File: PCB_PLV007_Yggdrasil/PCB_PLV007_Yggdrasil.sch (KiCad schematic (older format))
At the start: 26 parts, among them J1 Conn_01x12, U7 BME280, U8 SN65HVD232

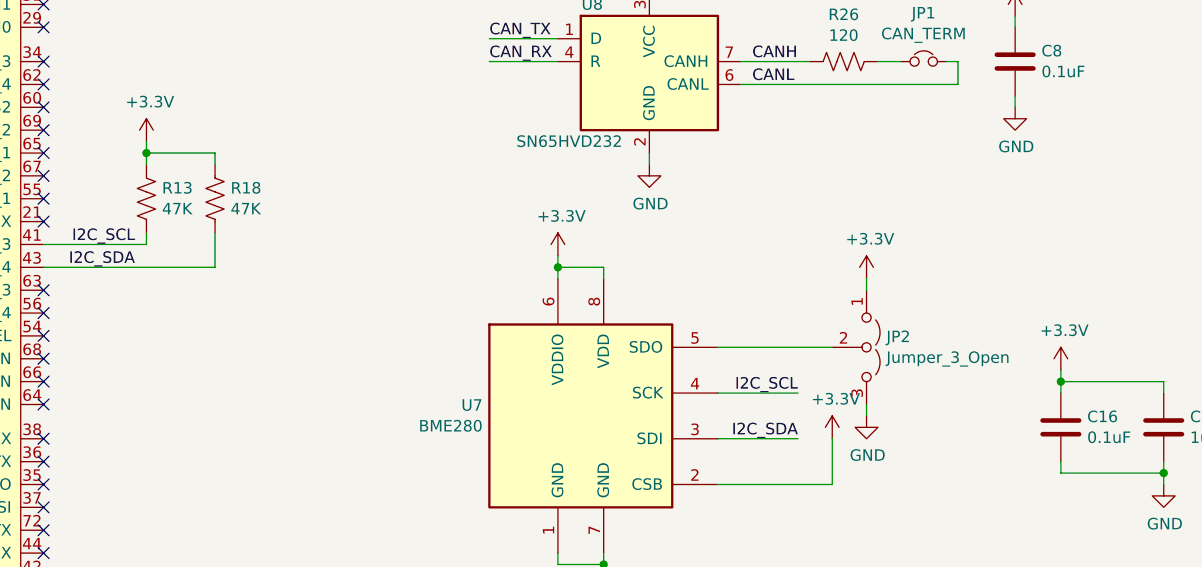
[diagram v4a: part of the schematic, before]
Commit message: Most of sensors for heimdal complete, still need to sort out load cells, flammable gas
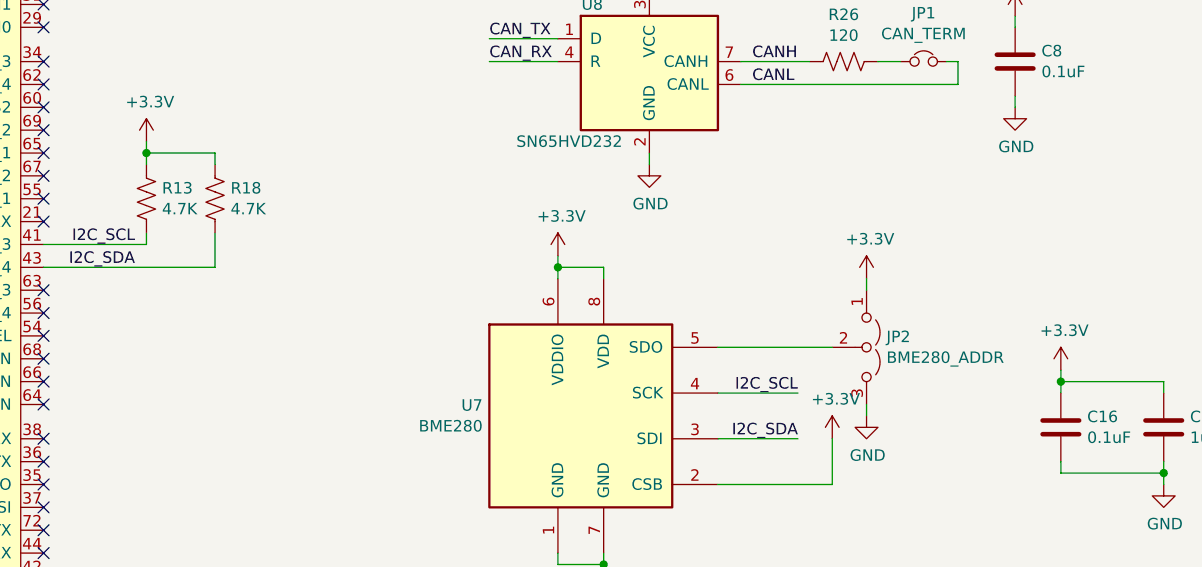
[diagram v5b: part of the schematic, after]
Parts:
- JP2: value Jumper_3_Open -> BME280_ADDR
- R13, R18: value 47K -> 4.7K
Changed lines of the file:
@@
 P 5500 4700
 F 0 "R13" H 5568 4746 50  0000 L CNN
-F 1 "47K" H 5568 4655 50  0000 L CNN
+F 1 "4.7K" H 5568 4655 50  0000 L CNN
 F 2 "" V 5540 4690 50  0001 C CNN
 F 3 "~" H 5500 4700 50  0001 C CNN
@@
 P 5800 4700
 F 0 "R18" H 5868 4746 50  0000 L CNN
-F 1 "47K" H 5868 4655 50  0000 L CNN
+F 1 "4.7K" H 5868 4655 50  0000 L CNN
 F 2 "" V 5840 4690 50  0001 C CNN
 F 3 "~" H 5800 4700 50  0001 C CNN
@@
 P 8650 5350
 F 0 "JP2" V 8604 5437 50  0000 L CNN
-F 1 "Jumper_3_Open" V 8695 5437 50  0000 L CNN
+F 1 "BME280_ADDR" V 8695 5437 50  0000 L CNN
 F 2 "" H 8650 5350 50  0001 C CNN
 F 3 "~" H 8650 5350 50  0001 C CNN

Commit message: Updates to Yggdrasil as per review by Fronk
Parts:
- added C22, C23: 10uF, symbol Device:C
- added R39, R40, R41, R42, R43, R44, R45: DNP, symbol Device:R_US
- C11, C12: value 1uF -> DNP
- C13: value 0.1uF -> 10uF
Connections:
- net +12V: now also C22.1, C23.1; no longer C11.1, C12.1
- net +28V: now also C11.1, C12.1
- net +3V3: now also R43.1, R44.1, R45.1; no longer U7.2 (CSB)
- net CAN_RX: now also R43.2
- net CAN_TX: now also R44.2
- net C_SAFE: now also NCLO1.59 (PA9/UART1_TX/PWM1_2)
- net GND: now also C22.2, C23.2
- net I2C_SCL: now also R39.1
- net I2C_SDA: now also R42.1
- net V_SAFE: now also NCLO1.61 (PA8/PWM1_1)
- net at NCLO1.54 (PB12/SPI2_SSEL): now also R40.2
- net at NCLO1.63 (PB10/I2C2_SCL/SPI2_SCLK/UART1_RX/UART3_TX/PWM2_3): now also R39.2
- net at NCLO1.64 (PB15/SPI2_MOSI/PWM1_3N): now also R42.2
- net at NCLO1.66 (PB14/I2C2_SDA/SPI2_MISO/PWM1_2N): now also R41.2
- net BME280_SDO: now reaches JP2.2 (C), U7.5 (SDO)
- net BME280_SDO: now also R41.1
- new net BME280_CSB: R40.1, R45.2, U7.2 (CSB)
- no-connect marks 48 -> 42

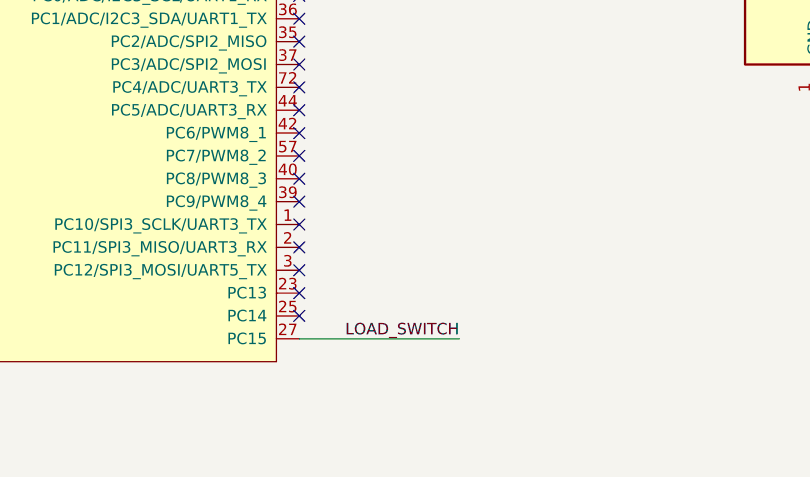
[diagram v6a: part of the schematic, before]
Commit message: Add heartbeat address lines to uC GPIO
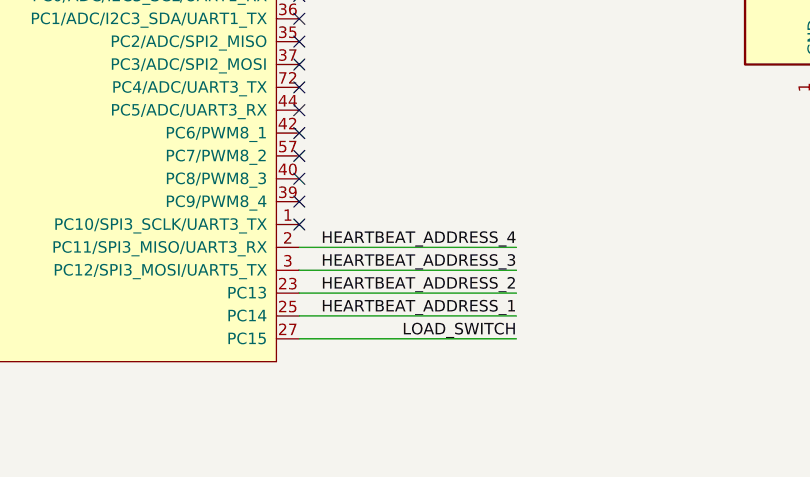
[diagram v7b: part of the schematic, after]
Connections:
- net HEARTBEAT_ADDRESS_1: now also NCLO1.25 (PC14)
- net HEARTBEAT_ADDRESS_2: now also NCLO1.23 (PC13)
- net HEARTBEAT_ADDRESS_3: now also NCLO1.3 (PC12/SPI3_MOSI/UART5_TX)
- net HEARTBEAT_ADDRESS_4: now also NCLO1.2 (PC11/SPI3_MISO/UART3_RX)
- no-connect marks 42 -> 38
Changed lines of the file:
@@
 Wire Wire Line
 	650  3850 1450 3850
-Text Label 5750 7250 2    50   ~ 0
+Text Label 6000 7250 2    50   ~ 0
 LOAD_SWITCH
 Wire Wire Line
-	5750 7250 5050 7250
+	6000 7250 5050 7250
 $Comp
 L Sensor:BME280 U7
@@
 NoConn ~ 5050 6650
 NoConn ~ 5050 6750
-NoConn ~ 5050 6850
-NoConn ~ 5050 6950
-NoConn ~ 5050 7050
-NoConn ~ 5050 7150
 NoConn ~ 1450 4250
 NoConn ~ 1450 4750
@@
 Text Label 650  4650 0    50   ~ 0
 C_SAFE
+Text Label 6000 6850 2    50   ~ 0
+HEARTBEAT_ADDRESS_4
+Wire Wire Line
+	6000 6850 5050 6850
+Text Label 6000 6950 2    50   ~ 0
+HEARTBEAT_ADDRESS_3
+Wire Wire Line
+	6000 6950 5050 6950
+Text Label 6000 7050 2    50   ~ 0
+HEARTBEAT_ADDRESS_2
+Wire Wire Line
+	6000 7050 5050 7050
+Text Label 6000 7150 2    50   ~ 0
+HEARTBEAT_ADDRESS_1
+Wire Wire Line
+	6000 7150 5050 7150
 $EndSCHEMATC

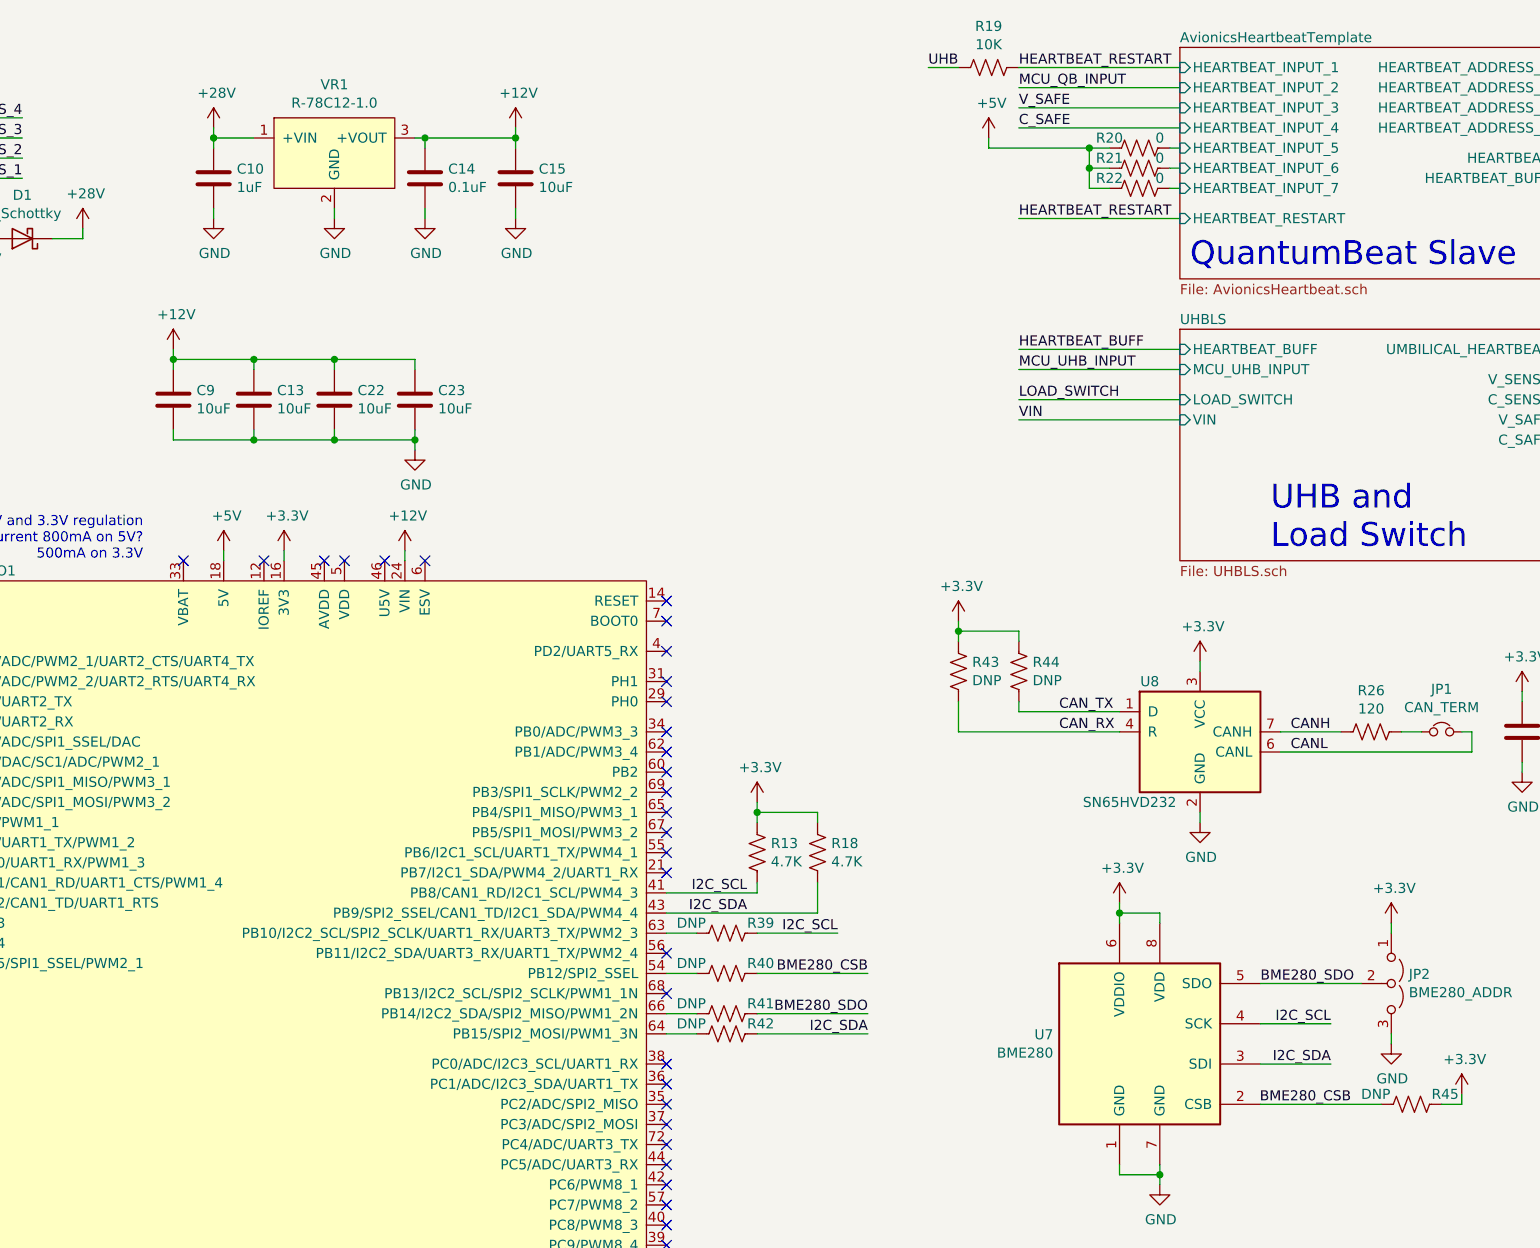
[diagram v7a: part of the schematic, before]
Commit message: Add power LEDs and large input caps to Yggdrasil, Odin
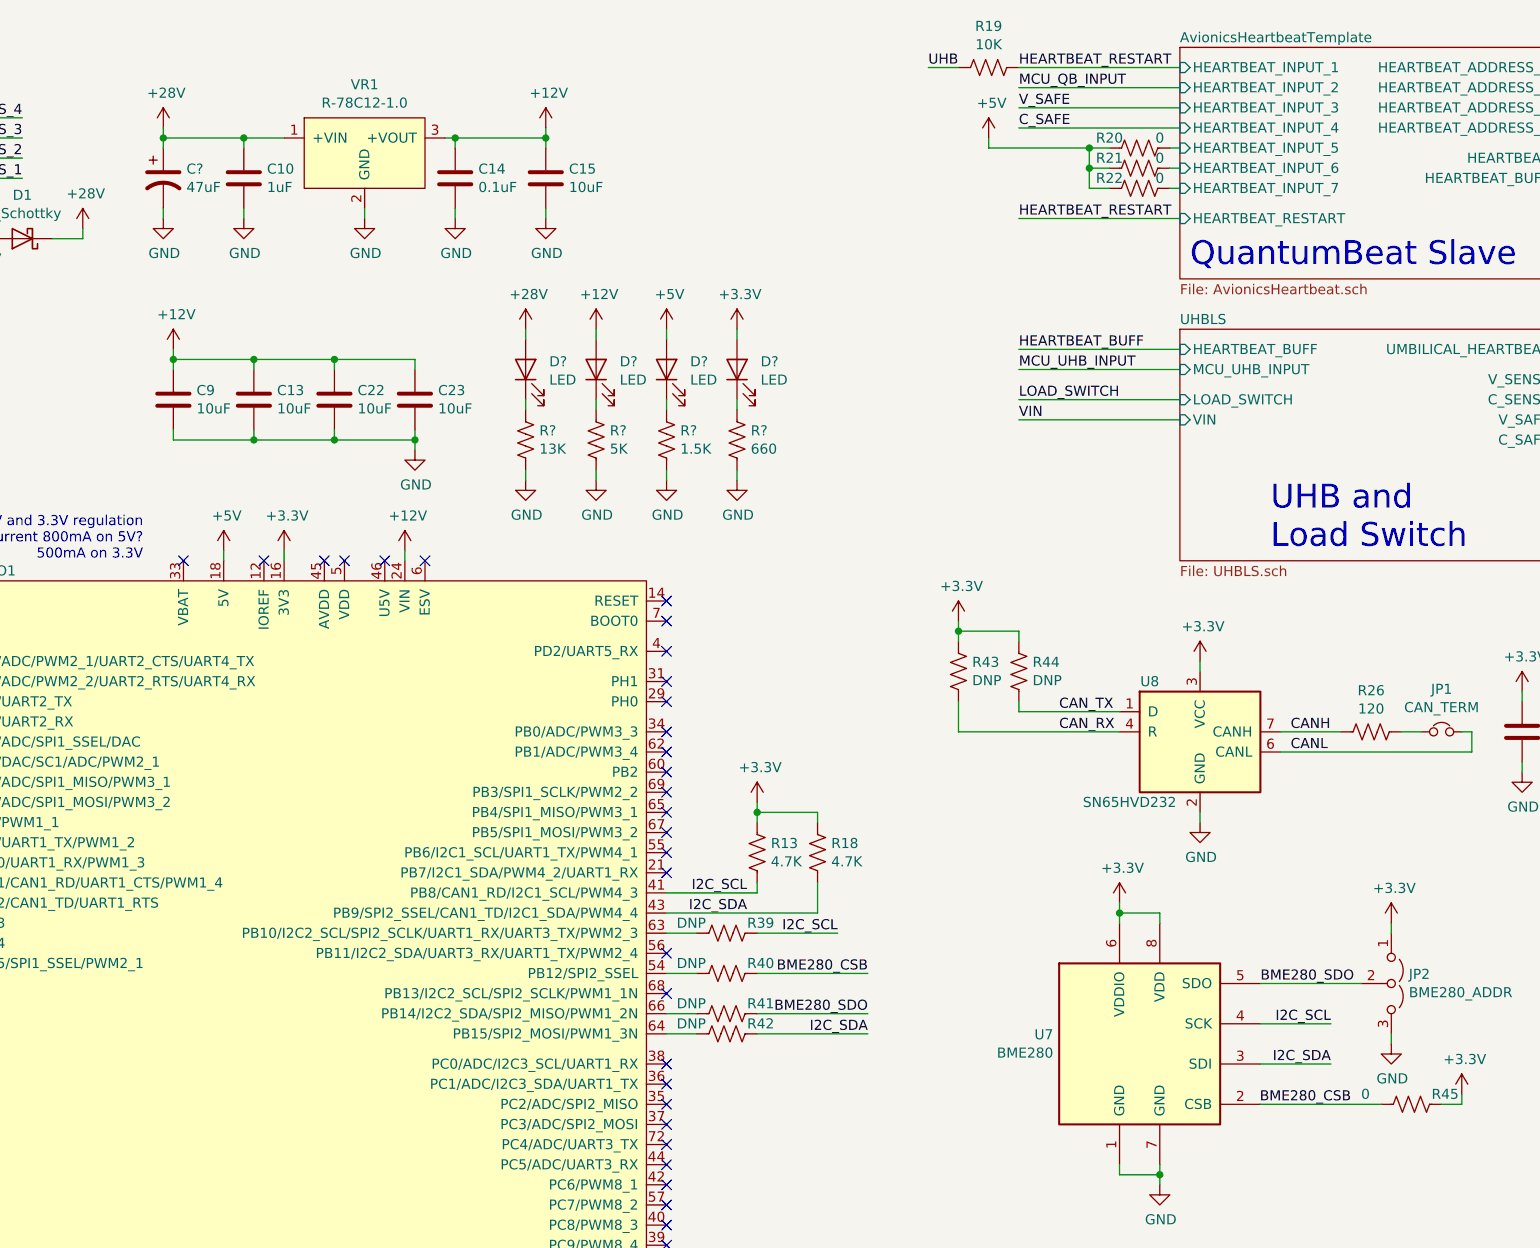
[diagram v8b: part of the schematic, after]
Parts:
- added C?: 47uF, symbol Device:CP1
- added D? (x4): LED, symbol Device:LED
- added R?: 13K, symbol Device:R_US
- added R?: 5K, symbol Device:R_US
- added R?: 1.5K, symbol Device:R_US
- added R?: 660, symbol Device:R_US
- R45: value DNP -> 0
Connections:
- net +12V: now also D?.2 (A)
- net +28V: now also C?.1, D?.2 (A)
- net +3V3: now also D?.2 (A)
- net +5V: now also D?.2 (A)
- net GND: now also C?.2, R?.2, R?.2, R?.2, R?.2
- new net: D?.1 (K), R?.1 (x4)
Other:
- moved on the sheet: C10, C14, C15, VR1
